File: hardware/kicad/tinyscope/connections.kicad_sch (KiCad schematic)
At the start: 0 parts

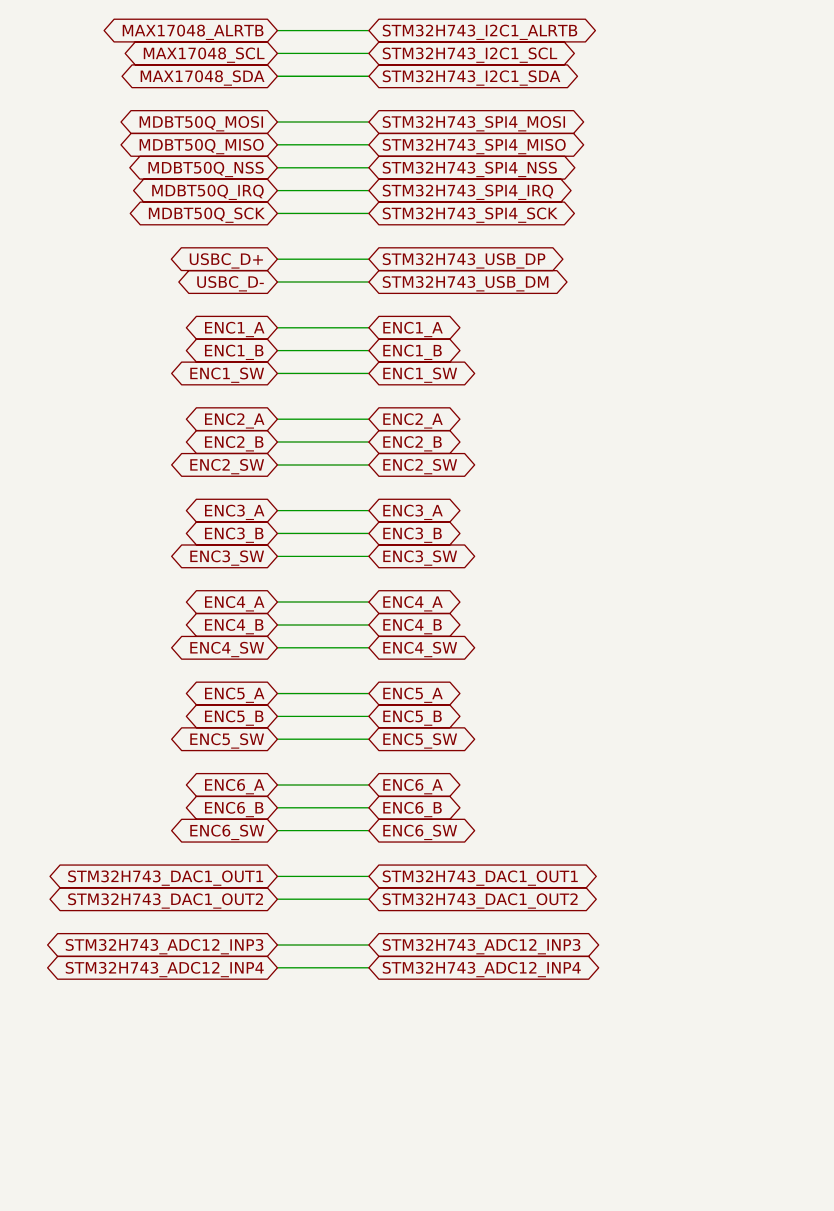
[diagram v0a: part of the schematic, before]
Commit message: feat: hardware: Add global labels on power and charging, and regulation and rails subschematics
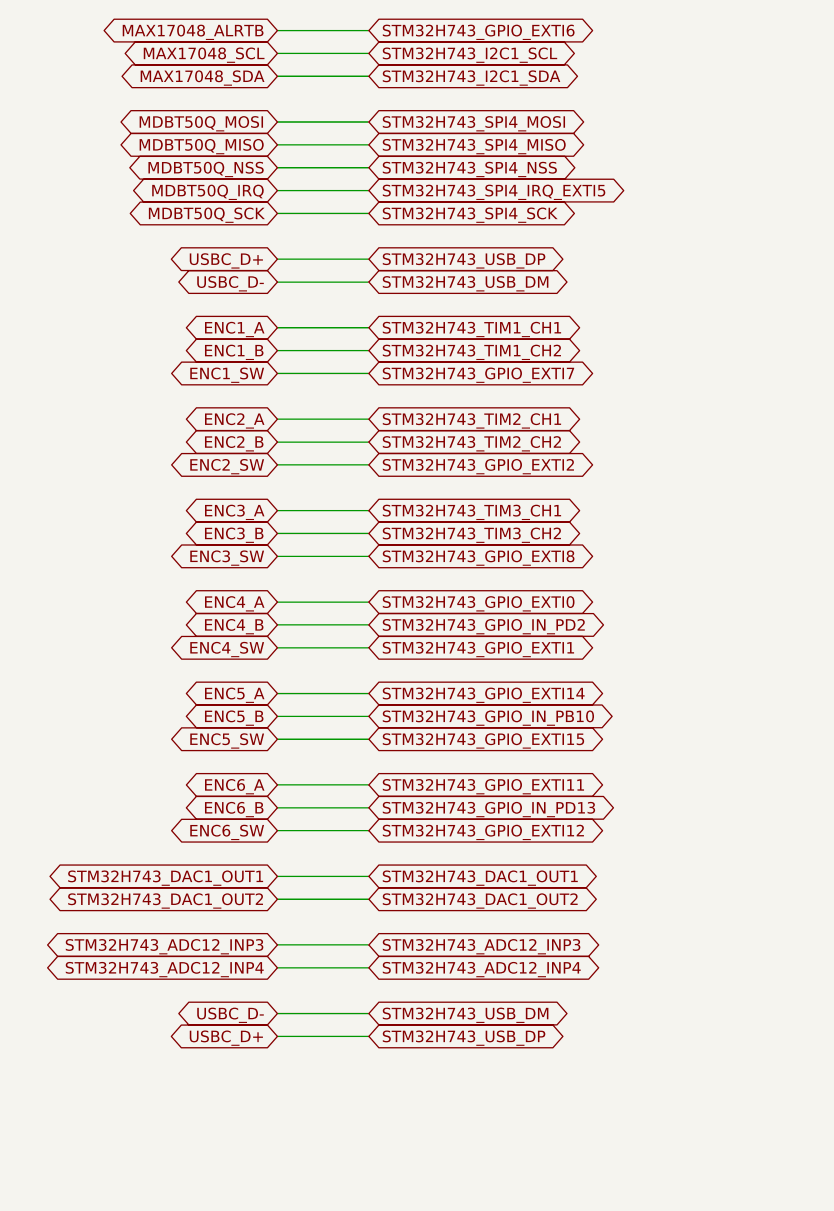
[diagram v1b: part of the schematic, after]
